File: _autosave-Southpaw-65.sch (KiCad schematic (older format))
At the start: 205 parts, among them J1 USB_C_Receptacle_USB2.0, SW1 SW_Push, U1 ATmega32A-PU, Y1 16MHz

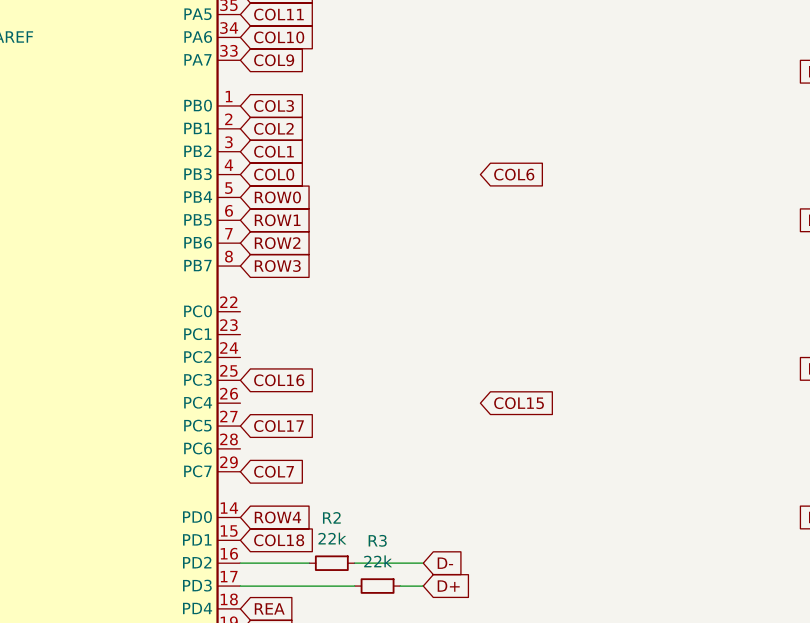
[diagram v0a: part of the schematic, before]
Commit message: Lots of wiring to MCU done
Considering redoing it because thicc bottom
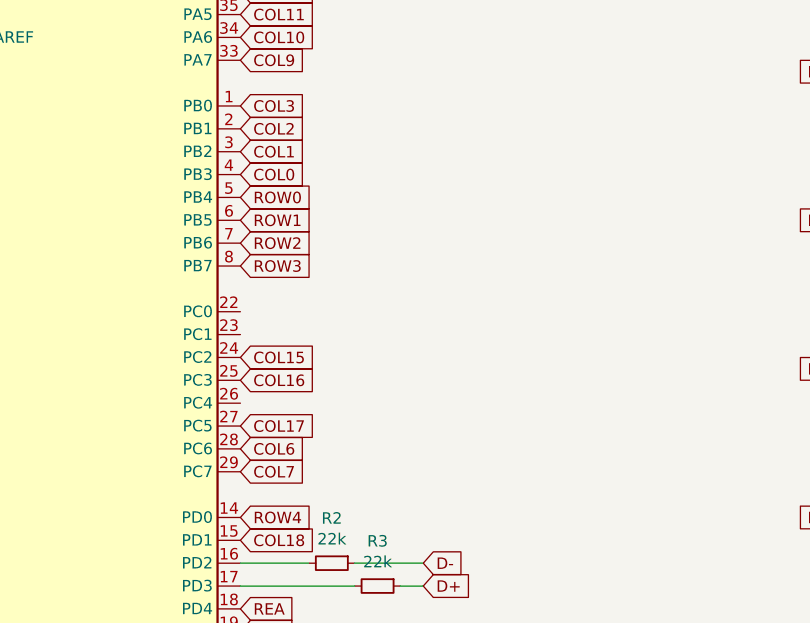
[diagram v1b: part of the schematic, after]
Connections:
- net COL15: now also U1.24 (PC2)
- net COL6: now also U1.28 (PC6)
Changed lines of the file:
@@
 Text GLabel 2000 1250 2    50   Input ~ 0
 COL14
-Text GLabel 3050 3250 2    50   Input ~ 0
+Text GLabel 2000 3050 2    50   Input ~ 0
 COL15
 Text GLabel 2000 3150 2    50   Input ~ 0
@@
 Text GLabel 2000 3550 2    50   Input ~ 0
 COL7
-Text GLabel 3050 2250 2    50   Input ~ 0
+Text GLabel 2000 3450 2    50   Input ~ 0
 COL6
 $EndSCHEMATC
